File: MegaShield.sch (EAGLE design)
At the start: 14 parts

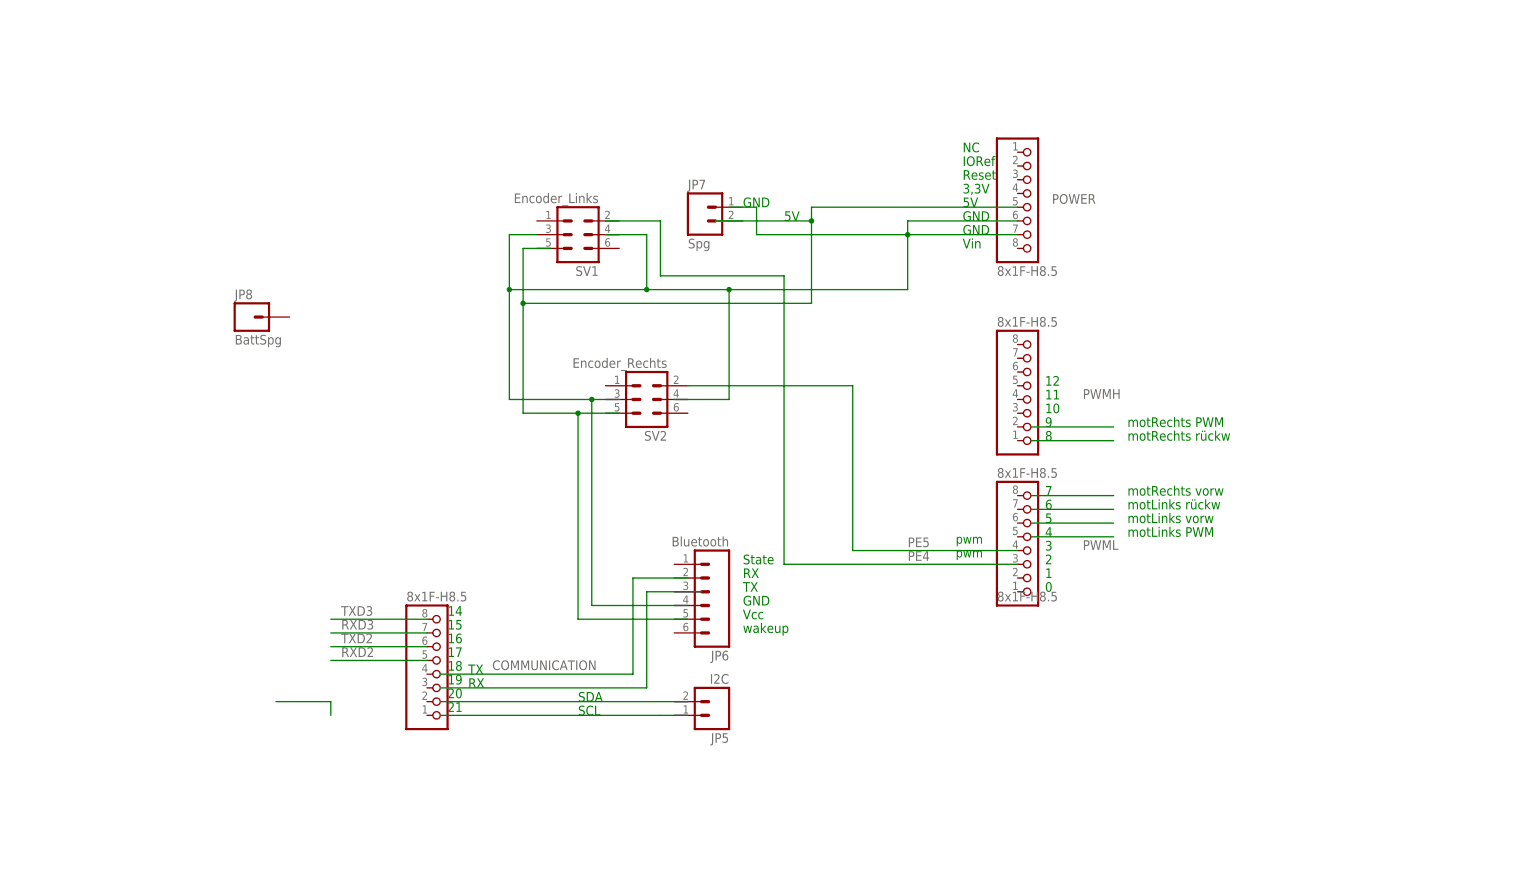
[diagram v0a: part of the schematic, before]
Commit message: 
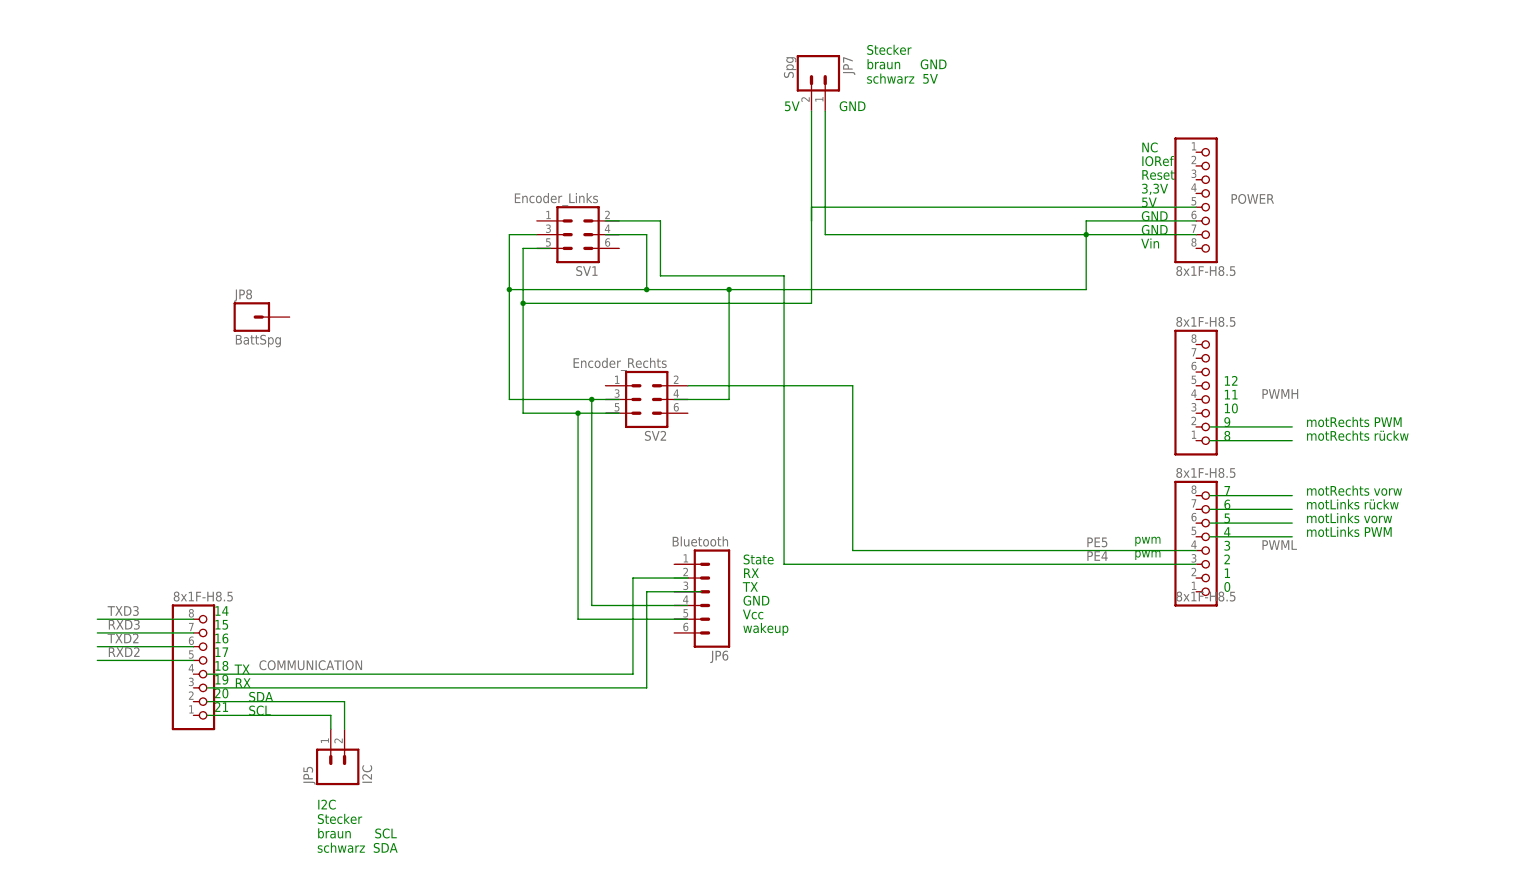
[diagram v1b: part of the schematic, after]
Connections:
- new net N$1: JP7.1
- new net N$11: JP5.1
- net N$2: now also JP7.2
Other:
- note added: "I2C Stecker braun SCL schwarz SDA"
- note added: "Stecker braun GND schwarz 5V"
- moved on the sheet: COMMUNICATION, JP5, JP7, POWER, PWMH, PWML

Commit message: 
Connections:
- net ADC4 renamed N$9
- removed net ADC0: ADCL.1
- removed net ADC1: ADCL.2
- removed net ADC2: ADCL.3
- removed net ADC3: ADCL.4
- removed net ADC5: ADCL.6
- removed net ADC6: ADCL.7
- removed net ADC7: ADCL.8
- removed net N$9 (its old number): POWER.5
- removed net RXD2: COMMUNICATION.5
- removed net RXD3: COMMUNICATION.7
- removed net TXD2: COMMUNICATION.6
- removed net TXD3: COMMUNICATION.8
- net N$1: now also POWER.5
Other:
- note added: "ADC0"
- note added: "ADC1"
- note added: "ADC2"
- note added: "ADC3"
- moved on the sheet: ADCL, JP8
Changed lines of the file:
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@@
 braun     GND
 schwarz  5V</text>
+<text x="-68.58" y="83.82" size="1.778" layer="91">ADC3</text>
+<text x="-68.58" y="91.44" size="1.778" layer="91">ADC0</text>
+<text x="-68.58" y="88.9" size="1.778" layer="91">ADC1</text>
+<text x="-68.58" y="86.36" size="1.778" layer="91">ADC2</text>
 </plain>
 <instances>
@@
 </instance>
 <instance part="JP7" gate="G$1" x="58.42" y="147.32" rot="R270"/>
-<instance part="JP8" gate="G$1" x="-45.72" y="101.6"/>
+<instance part="JP8" gate="G$1" x="-78.74" y="83.82"/>
 <instance part="PWML" gate="A" x="132.08" y="60.96" smashed="yes" rot="MR180">
 <attribute name="NAME" x="141.605" y="60.325" size="1.778" layer="95" rot="MR180"/>
 <attribute name="VALUE" x="125.73" y="73.66" size="1.778" layer="96" rot="MR180"/>
 </instance>
-<instance part="ADCL" gate="A" x="261.62" y="48.26" smashed="yes" rot="MR180">
-<attribute name="NAME" x="271.145" y="50.165" size="1.778" layer="95" rot="MR180"/>
-<attribute name="VALUE" x="125.73" y="50.8" size="1.778" layer="96" rot="MR180"/>
+<instance part="ADCL" gate="A" x="-53.34" y="83.82" smashed="yes" rot="MR180">
+<attribute name="NAME" x="-43.815" y="85.725" size="1.778" layer="95" rot="MR180"/>
+<attribute name="VALUE" x="-189.23" y="86.36" size="1.778" layer="96" rot="MR180"/>
 </instance>
 <instance part="COMMUNICATION" gate="A" x="-53.34" y="38.1" smashed="yes" rot="MR180">
@@
 </segment>
 </net>
-<net name="ADC0" class="0">
-<segment>
-<wire x1="259.08" y1="38.1" x2="203.2" y2="38.1" width="0.1524" layer="91"/>
-<label x="242.57" y="40.64" size="1.778" layer="95" rot="MR180"/>
-<pinref part="ADCL" gate="A" pin="1"/>
-</segment>
-</net>
-<net name="ADC2" class="0">
-<segment>
-<wire x1="259.08" y1="43.18" x2="203.2" y2="43.18" width="0.1524" layer="91"/>
-<label x="242.57" y="45.72" size="1.778" layer="95" rot="MR180"/>
-<pinref part="ADCL" gate="A" pin="3"/>
-</segment>
-</net>
-<net name="ADC1" class="0">
-<segment>
-<wire x1="203.2" y1="40.64" x2="259.08" y2="40.64" width="0.1524" layer="91"/>
-<label x="242.57" y="43.18" size="1.778" layer="95" rot="MR180"/>
-<pinref part="ADCL" gate="A" pin="2"/>
-</segment>
-</net>
-<net name="ADC3" class="0">
-<segment>
-<wire x1="203.2" y1="45.72" x2="259.08" y2="45.72" width="0.1524" layer="91"/>
-<label x="242.57" y="48.26" size="1.778" layer="95" rot="MR180"/>
-<pinref part="ADCL" gate="A" pin="4"/>
-</segment>
-</net>
-<net name="ADC4" class="0">
-<segment>
-<wire x1="259.08" y1="48.26" x2="203.2" y2="48.26" width="0.1524" layer="91"/>
-<label x="242.57" y="50.8" size="1.778" layer="95" rot="MR180"/>
-<pinref part="ADCL" gate="A" pin="5"/>
-</segment>
-</net>
-<net name="ADC5" class="0">
-<segment>
-<wire x1="203.2" y1="50.8" x2="259.08" y2="50.8" width="0.1524" layer="91"/>
-<label x="242.57" y="53.34" size="1.778" layer="95" rot="MR180"/>
-<pinref part="ADCL" gate="A" pin="6"/>
-</segment>
-</net>
-<net name="ADC6" class="0">
-<segment>
-<wire x1="203.2" y1="53.34" x2="259.08" y2="53.34" width="0.1524" layer="91"/>
-<label x="242.57" y="55.88" size="1.778" layer="95" rot="MR180"/>
-<pinref part="ADCL" gate="A" pin="7"/>
-</segment>
-</net>
-<net name="ADC7" class="0">
-<segment>
-<wire x1="259.08" y1="55.88" x2="203.2" y2="55.88" width="0.1524" layer="91"/>
-<label x="242.57" y="58.42" size="1.778" layer="95" rot="MR180"/>
-<pinref part="ADCL" gate="A" pin="8"/>
-</segment>
-</net>
 <net name="SDA" class="0">
 <segment>
@@
 <label x="240.03" y="132.715" size="1.778" layer="95"/>
 <pinref part="JP11" gate="A" pin="9"/>
-</segment>
-</net>
-<net name="RXD2" class="0">
-<segment>
-<wire x1="-73.66" y1="38.1" x2="-55.88" y2="38.1" width="0.1524" layer="91"/>
-<label x="-71.755" y="38.735" size="1.778" layer="95"/>
-<pinref part="COMMUNICATION" gate="A" pin="5"/>
-</segment>
-</net>
-<net name="RXD3" class="0">
-<segment>
-<wire x1="-73.66" y1="43.18" x2="-55.88" y2="43.18" width="0.1524" layer="91"/>
-<label x="-71.755" y="43.815" size="1.778" layer="95"/>
-<pinref part="COMMUNICATION" gate="A" pin="7"/>
-</segment>
-</net>
-<net name="TXD2" class="0">
-<segment>
-<wire x1="-73.66" y1="40.64" x2="-55.88" y2="40.64" width="0.1524" layer="91"/>
-<label x="-71.755" y="41.275" size="1.778" layer="95"/>
-<pinref part="COMMUNICATION" gate="A" pin="6"/>
-</segment>
-</net>
-<net name="TXD3" class="0">
-<segment>
-<wire x1="-55.88" y1="45.72" x2="-73.66" y2="45.72" width="0.1524" layer="91"/>
-<label x="-71.755" y="46.355" size="1.778" layer="95"/>
-<pinref part="COMMUNICATION" gate="A" pin="8"/>
 </segment>
 </net>
@@
 <net name="N$1" class="3">
 <segment>
-<wire x1="58.42" y1="104.14" x2="58.42" y2="139.7" width="0.1524" layer="91"/>
+<wire x1="58.42" y1="104.14" x2="58.42" y2="121.92" width="0.1524" layer="91"/>
+<wire x1="58.42" y1="121.92" x2="58.42" y2="139.7" width="0.1524" layer="91"/>
 <wire x1="10.16" y1="114.3" x2="5.08" y2="114.3" width="0.1524" layer="91"/>
 <wire x1="5.08" y1="114.3" x2="5.08" y2="104.14" width="0.1524" layer="91"/>
@@
 <junction x="15.24" y="83.82"/>
 <pinref part="JP7" gate="G$1" pin="1"/>
+<pinref part="POWER" gate="A" pin="5"/>
+<wire x1="129.54" y1="121.92" x2="58.42" y2="121.92" width="0.1524" layer="91"/>
+<wire x1="58.42" y1="121.92" x2="58.42" y2="119.38" width="0.1524" layer="91"/>
+<junction x="58.42" y="121.92"/>
 </segment>
 </net>
@@
 </segment>
 </net>
-<net name="N$9" class="3">
-<segment>
-<pinref part="POWER" gate="A" pin="5"/>
-<wire x1="129.54" y1="121.92" x2="58.42" y2="121.92" width="0.1524" layer="91"/>
-<wire x1="58.42" y1="121.92" x2="58.42" y2="119.38" width="0.1524" layer="91"/>
-</segment>
-</net>
+<net name="N$9" class="0">
+<segment>
+<pinref part="ADCL" gate="A" pin="5"/>
+<wire x1="-55.88" y1="83.82" x2="-73.66" y2="83.82" width="0.1524" layer="91"/>
+</segment>
+</net>

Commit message: 
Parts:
- removed ADCH: 8x1F-H8.5, SmartPrj:PINHD-1X8
- removed JP11: 10x1F-H8.5, SmartPrj:PINHD-1X10_ARD
- removed XIO: 18x2F-H8.5, SmartPrj:PINHD-2X18
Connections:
- removed net +5V: XIO.1, XIO.2
- removed net ADC10: ADCH.3
- removed net ADC11: ADCH.4
- removed net ADC12: ADCH.5
- removed net ADC13: ADCH.6
- removed net ADC14: ADCH.7
- removed net ADC15: ADCH.8
- removed net ADC8: ADCH.1
- removed net ADC9: ADCH.2
- removed net AREF: JP11.3
- removed net GND: JP11.4, XIO.35, XIO.36
- removed net PA0: XIO.3
- removed net PA1: XIO.4
- removed net PA2: XIO.5
- removed net PA3: XIO.6
- removed net PA4: XIO.7
- removed net PA5: XIO.8
- removed net PA6: XIO.9
- removed net PA7: XIO.10
- removed net PB0: XIO.34
- removed net PB1: XIO.33
- removed net PB2: XIO.32
- removed net PB3: XIO.31
- removed net PB4: JP11.8
- removed net PB5: JP11.7
- removed net PB6: JP11.6
- removed net PB7: JP11.5
- removed net PC0: XIO.18
- removed net PC1: XIO.17
- removed net PC2: XIO.16
- removed net PC3: XIO.15
- removed net PC4: XIO.14
- removed net PC5: XIO.13
- removed net PC6: XIO.12
- removed net PC7: XIO.11
- removed net PD7: XIO.19
- removed net PG0: XIO.22
- removed net PG1: XIO.21
- removed net PG2: XIO.20
- removed net PH5: JP11.10
- removed net PH6: JP11.9
- removed net PL0: XIO.30
- removed net PL1: XIO.29
- removed net PL2: XIO.28
- removed net PL3: XIO.27
- removed net PL4: XIO.26
- removed net PL5: XIO.25
- removed net PL6: XIO.24
- removed net PL7: XIO.23
- removed net SCL: JP11.1
- removed net SDA: JP11.2
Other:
- note removed: "(MISO)"
- note removed: "(MOSI)"
- note removed: "(SCK)"
- note removed: "(SS)"
- note removed: "13"
- note removed: "22"
- note removed: "23"
- note removed: "24"
- note removed: "25"
- note removed: "26"
- note removed: "27"
- note removed: "28"
- note removed: "29"
- note removed: "30"
- note removed: "31"
- note removed: "32"
- note removed: "33"
- note removed: "34"
- note removed: "35"
- note removed: "36"
- note removed: "37"
- note removed: "38"
- note removed: "39"
- note removed: "40"
- note removed: "41"
- note removed: "42"
- note removed: "43"
- note removed: "44"
- note removed: "45"
- note removed: "46"
- note removed: "47"
- note removed: "48"
- note removed: "49"
- note removed: "50"
- note removed: "51"
- note removed: "52"
- note removed: "53"

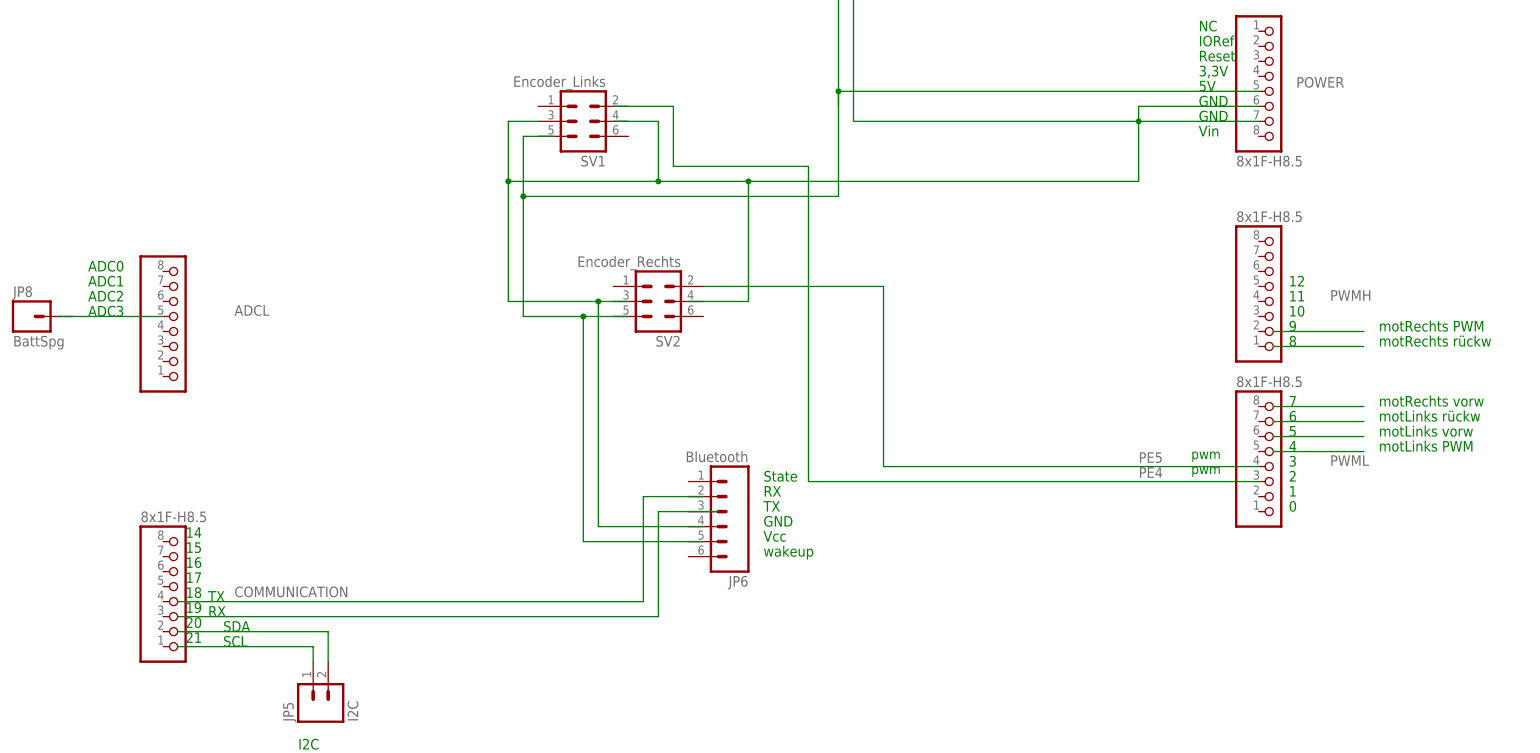
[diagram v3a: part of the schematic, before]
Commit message: 
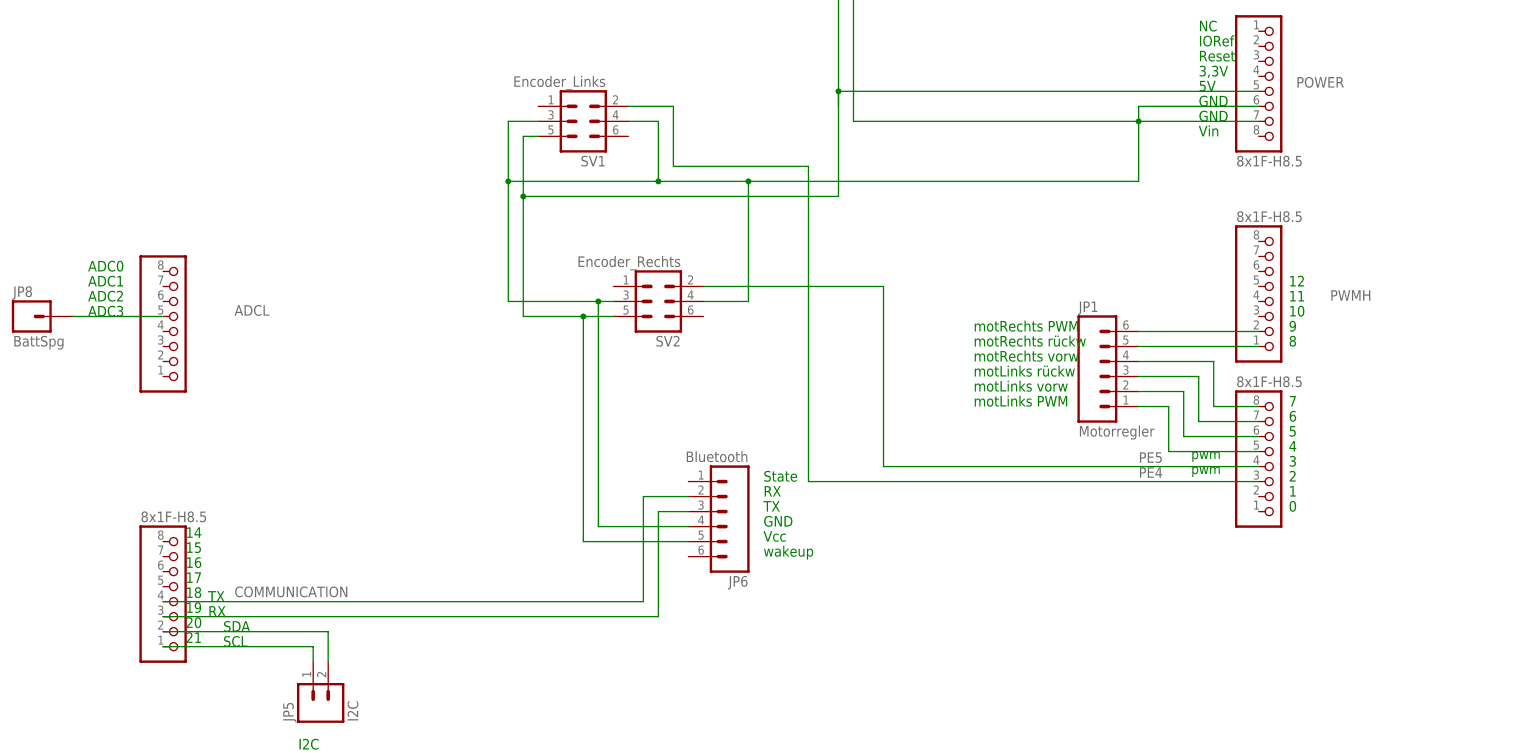
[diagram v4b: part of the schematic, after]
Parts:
- added JP1: Motorregler, SparkFun-Connectors:M06LOCK
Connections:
- removed net N$9: ADCL.5
- new net N$12: COMMUNICATION.3, JP6.3
- new net N$13: COMMUNICATION.4, JP6.2
- new net N$16: JP1.4, PWML.8
- new net N$17: JP1.3, PWML.7
- new net N$18: JP1.2, PWML.6
- new net N$19: JP1.1, PWML.5
- new net N$3: JP1.6, PWMH.2
- new net N$4: JP1.5, PWMH.1
- new net N$5: ADCL.5, JP8.1
- net N$1: now also JP6.5, SV1.5, SV2.5
- net N$10: now also COMMUNICATION.1
- net N$11: now also COMMUNICATION.2
- net N$2: now also JP6.4, SV1.4, SV2.3, SV2.4
- net PE4: now also SV1.2
